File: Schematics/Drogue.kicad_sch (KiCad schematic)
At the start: 7 parts, among them J1 Pyro, Q1 BSC098N10NS5, Q3 NMOS

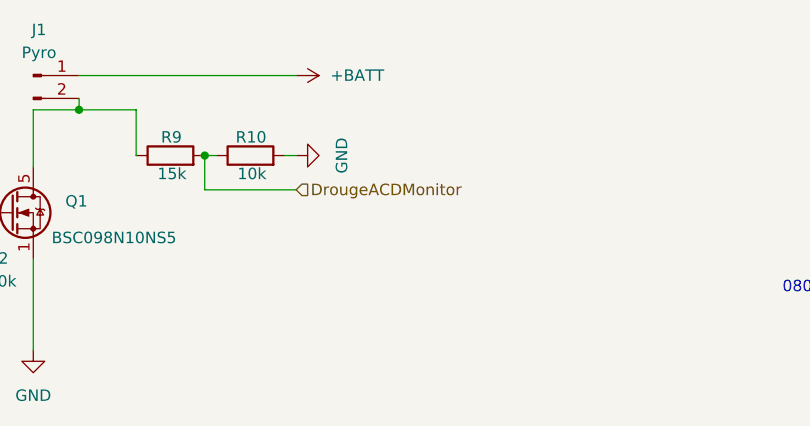
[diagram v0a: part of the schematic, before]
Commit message: finished sensor schematics, added datasheets organized files
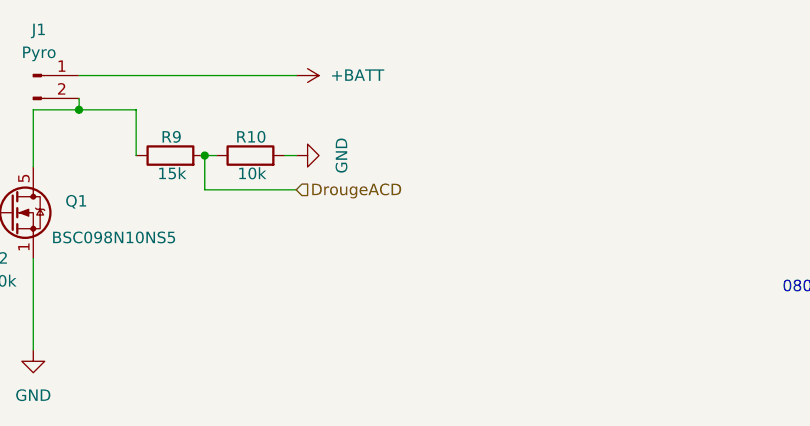
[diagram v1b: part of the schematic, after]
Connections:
- net DrougeACDMonitor renamed DrougeACD
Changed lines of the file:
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@@
 		)
 	)
-	(hierarchical_label "DrougeACDMonitor"
+	(hierarchical_label "DrougeACD"
 		(shape input)
 		(at 160.02 73.66 0)

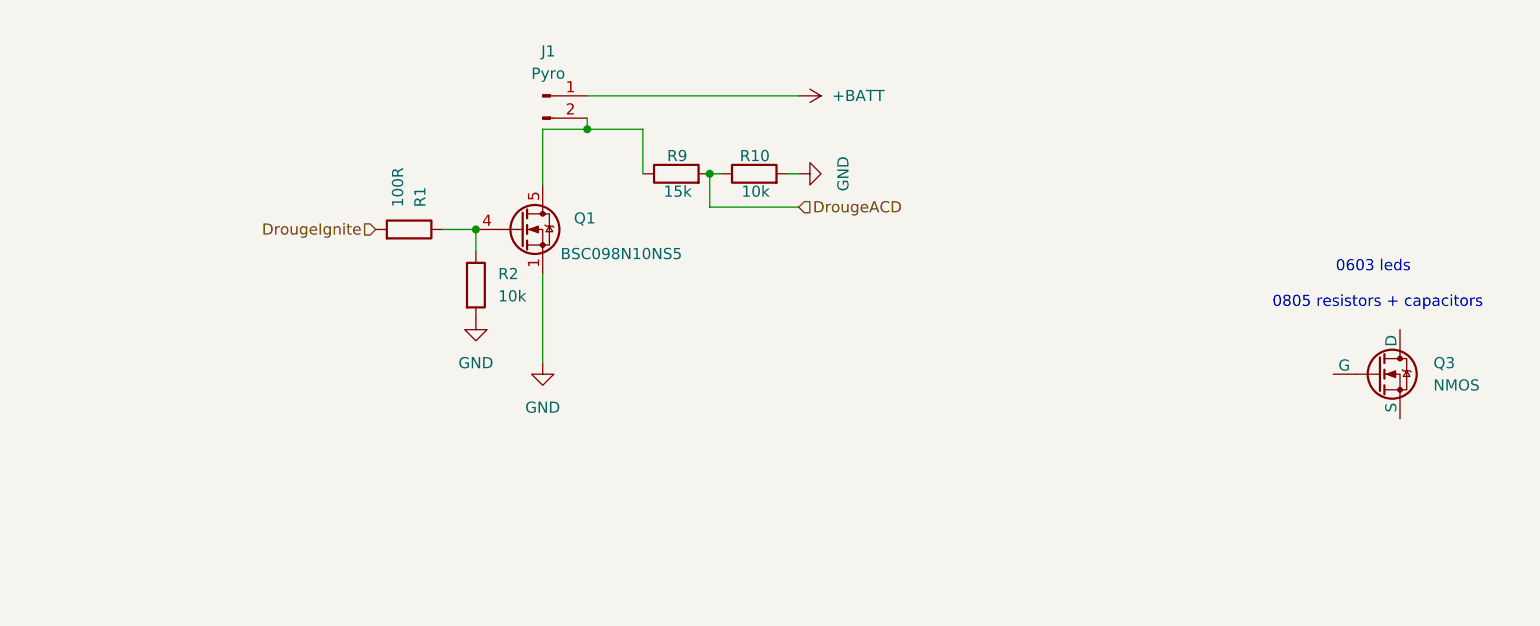
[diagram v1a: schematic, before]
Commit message: added LCSC numbers and footprint values, need to connect schemeatic pins, then can start layout
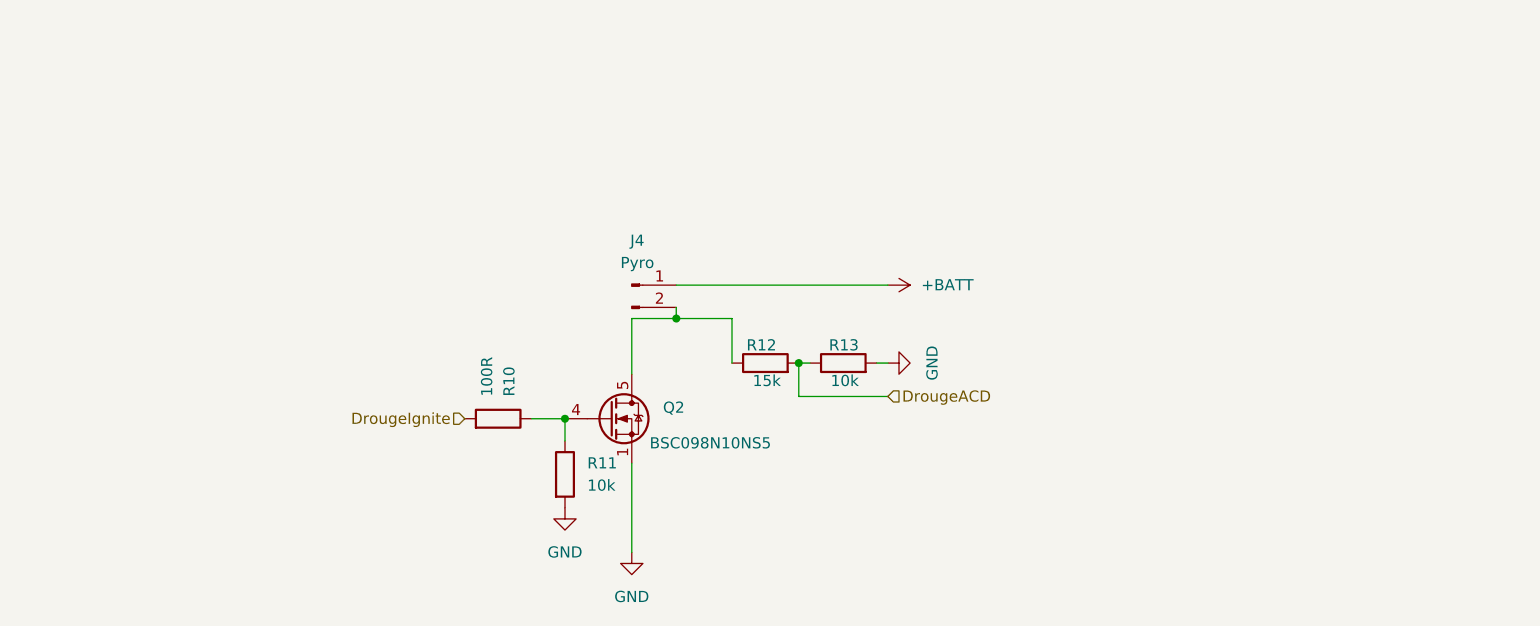
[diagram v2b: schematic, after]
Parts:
- removed Q3: NMOS, symbol Simulation_SPICE:NMOS
- J4: renamed from J1; footprint Connector_Molex:Molex_KK-254_AE-6410-02A_1x02_P2.54mm_Vertical -> myFootprints:MOLEX_26013114; LCSC Part (none) -> C17644051
- Q2: renamed from Q1; LCSC Part (none) -> C534398
- R10: renamed from R1; LCSC Part (none) -> C17408
- R11: renamed from R2; LCSC Part (none) -> C84376
- R12: renamed from R9; footprint Resistor_SMD:R_0805_2012Metric -> Resistor_SMD:R_0805_2012Metric_Pad1.20x1.40mm_HandSolder; LCSC Part (none) -> C2930170
- R13: renamed from R10; LCSC Part (none) -> C84376
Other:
- note removed: "0603 leds"
- note removed: "0805 resistors + capacitors"
- moved on the sheet: J4, Q2, R10, R11, R12, R13

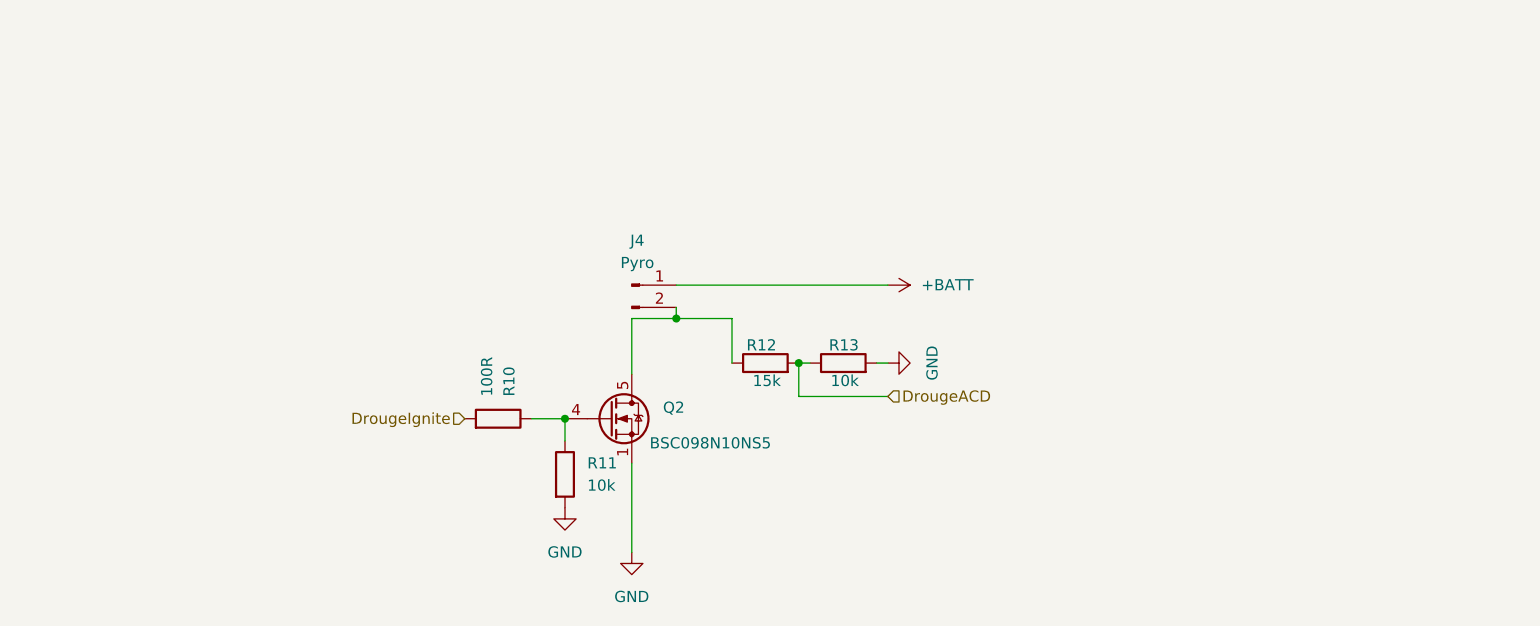
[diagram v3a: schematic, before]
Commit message: fixed symbols and added diodes to power input before ldo
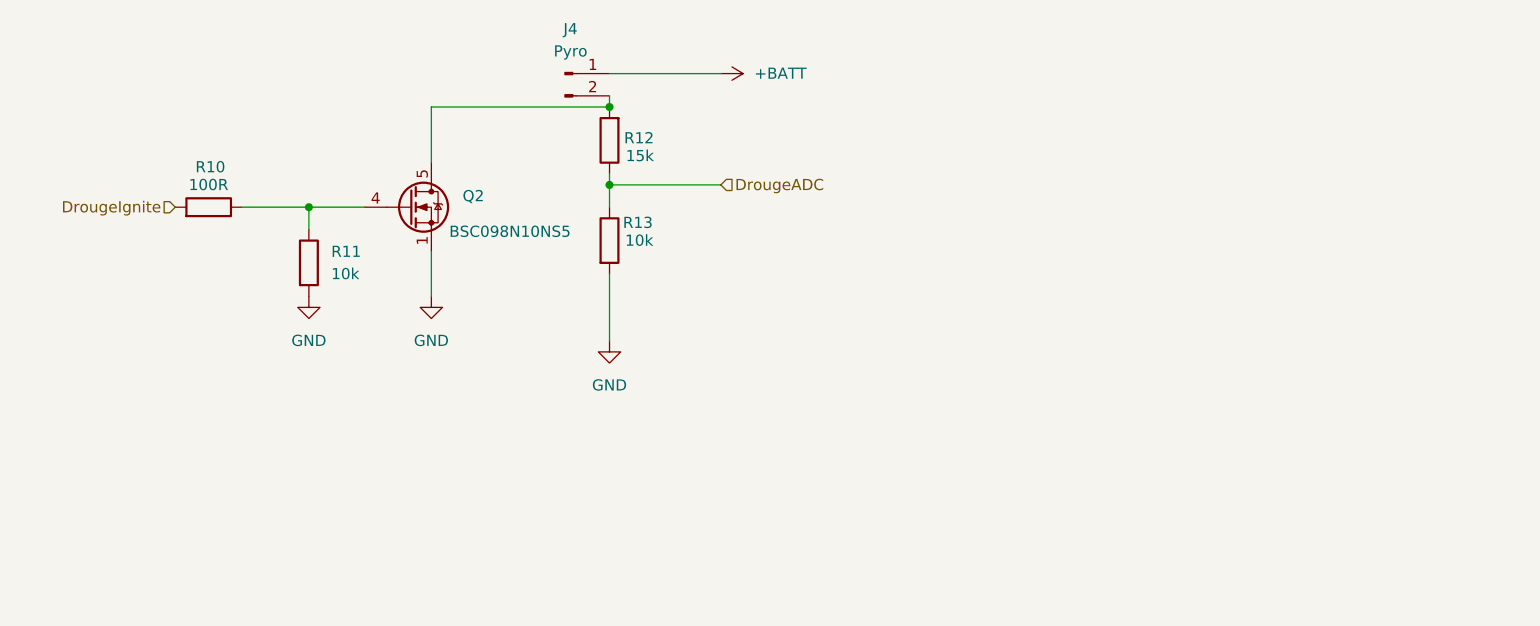
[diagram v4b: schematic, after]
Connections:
- net at J4.2 (Pin_2), Q2.5 (D): now also R12.2; no longer R12.1
- net DrougeACD renamed DrougeADC
- net DrougeADC: now also R12.1; no longer R12.2
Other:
- moved on the sheet: J4, Q2, R10, R11, R12, R13

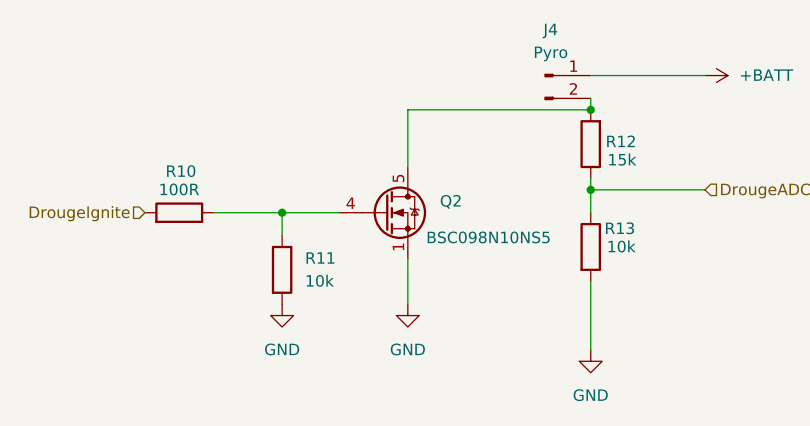
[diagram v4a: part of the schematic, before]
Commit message: added lora correct and organizing sheet pins
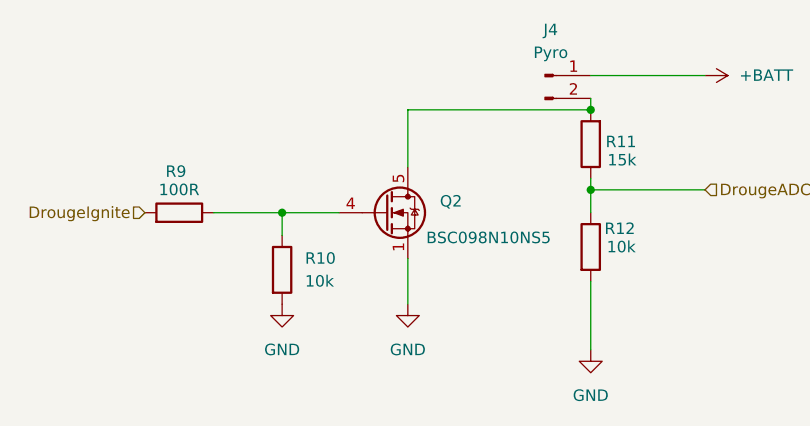
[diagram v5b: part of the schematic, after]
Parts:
- renumbered R11 to R10, R12 to R11, R13 to R12, R10 to R9
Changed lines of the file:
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@@
 		(on_board yes)
 		(dnp no)
-		(property "Reference" "R12"
+		(property "Reference" "R11"
 			(at 143.51 65.786 0)
 			(effects
@@
 			(project "flightcomputer2"
 				(path "/6cb3dda3-5fe8-4715-b831-354360aa3199/49edfe84-9da0-4fce-8baf-f24126c92814"
-					(reference "R12")
+					(reference "R11")
 					(unit 1)
 				)
@@
 		(on_board yes)
 		(dnp no)
-		(property "Reference" "R10"
+		(property "Reference" "R9"
 			(at 91.186 69.088 90)
 			(effects
@@
 			(project "flightcomputer2"
 				(path "/6cb3dda3-5fe8-4715-b831-354360aa3199/49edfe84-9da0-4fce-8baf-f24126c92814"
-					(reference "R10")
+					(reference "R9")
 					(unit 1)
 				)
@@
 		(dnp no)
 		(fields_autoplaced yes)
-		(property "Reference" "R11"
+		(property "Reference" "R10"
 			(at 106.68 78.7399 0)
 			(effects
@@
 			(project "flightcomputer2"
 				(path "/6cb3dda3-5fe8-4715-b831-354360aa3199/49edfe84-9da0-4fce-8baf-f24126c92814"
-					(reference "R11")
+					(reference "R10")
 					(unit 1)
 				)
@@
 		(dnp no)
 		(fields_autoplaced yes)
-		(property "Reference" "#PWR050"
+		(property "Reference" "#PWR047"
 			(at 138.43 95.25 0)
 			(effects
@@
 			(project "flightcomputer2"
 				(path "/6cb3dda3-5fe8-4715-b831-354360aa3199/49edfe84-9da0-4fce-8baf-f24126c92814"
-					(reference "#PWR050")
+					(reference "#PWR047")
 					(unit 1)
 				)
@@
 		(on_board yes)
 		(dnp no)
-		(property "Reference" "R13"
+		(property "Reference" "R12"
 			(at 139.954 75.438 0)
 			(effects
@@
 			(project "flightcomputer2"
 				(path "/6cb3dda3-5fe8-4715-b831-354360aa3199/49edfe84-9da0-4fce-8baf-f24126c92814"
-					(reference "R13")
-					(unit 1)
-				)
+					(reference "R12")
+					(unit 1)
+				)

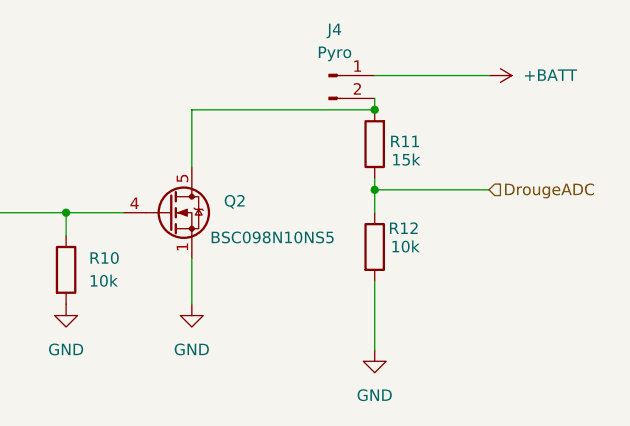
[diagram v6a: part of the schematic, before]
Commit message: first layout need to go over schematic
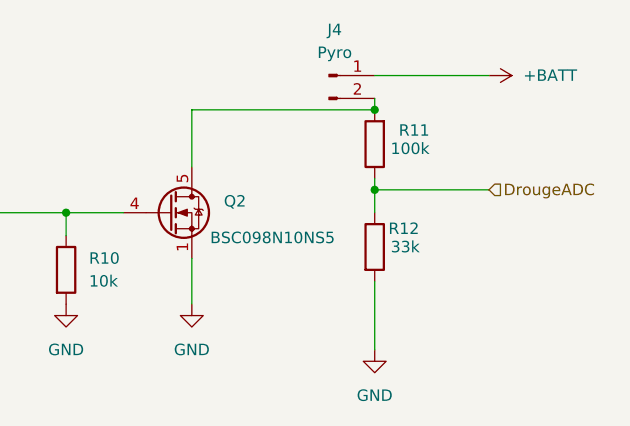
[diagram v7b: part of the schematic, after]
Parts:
- R10, R9: footprint Resistor_SMD:R_0805_2012Metric -> Resistor_SMD:R_0805_2012Metric_Pad1.20x1.40mm_HandSolder
- R11: value 15k -> 100k; LCSC Part C2930170 -> C96346
- R12: value 10k -> 33k; footprint Resistor_SMD:R_0805_2012Metric -> Resistor_SMD:R_0805_2012Metric_Pad1.20x1.40mm_HandSolder; LCSC Part C84376 -> C2933415
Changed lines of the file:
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@@
 		(dnp no)
 		(fields_autoplaced yes)
-		(property "Reference" "#PWR046"
+		(property "Reference" "#PWR052"
 			(at 118.11 90.17 0)
 			(effects
@@
 			(project "flightcomputer2"
 				(path "/6cb3dda3-5fe8-4715-b831-354360aa3199/49edfe84-9da0-4fce-8baf-f24126c92814"
-					(reference "#PWR046")
+					(reference "#PWR052")
 					(unit 1)
 				)
@@
 		(dnp no)
 		(property "Reference" "R11"
-			(at 143.51 65.786 0)
-			(effects
-				(font
-					(size 1.27 1.27)
-				)
-				(justify left)
-			)
-		)
-		(property "Value" "15k"
-			(at 143.51 67.818 0)
+			(at 144.526 64.516 0)
+			(effects
+				(font
+					(size 1.27 1.27)
+				)
+				(justify left)
+			)
+		)
+		(property "Value" "100k"
+			(at 144.526 66.548 0)
 			(effects
 				(font
@@
 			)
 		)
-		(property "LCSC Part" "C2930170"
+		(property "LCSC Part" "C96346"
 			(at 138.43 66.04 90)
 			(effects
@@
 			)
 		)
-		(property "Footprint" "Resistor_SMD:R_0805_2012Metric"
+		(property "Footprint" "Resistor_SMD:R_0805_2012Metric_Pad1.20x1.40mm_HandSolder"
 			(at 92.71 75.438 90)
 			(effects
@@
 			)
 		)
-		(property "Footprint" "Resistor_SMD:R_0805_2012Metric"
+		(property "Footprint" "Resistor_SMD:R_0805_2012Metric_Pad1.20x1.40mm_HandSolder"
 			(at 102.362 80.01 90)
 			(effects
@@
 		(dnp no)
 		(fields_autoplaced yes)
-		(property "Reference" "#PWR047"
+		(property "Reference" "#PWR053"
 			(at 138.43 95.25 0)
 			(effects
@@
 			(project "flightcomputer2"
 				(path "/6cb3dda3-5fe8-4715-b831-354360aa3199/49edfe84-9da0-4fce-8baf-f24126c92814"
-					(reference "#PWR047")
+					(reference "#PWR053")
 					(unit 1)
 				)
@@
 		(dnp no)
 		(fields_autoplaced yes)
-		(property "Reference" "#PWR049"
+		(property "Reference" "#PWR055"
 			(at 147.32 58.42 0)
 			(effects
@@
 			(project ""
 				(path "/6cb3dda3-5fe8-4715-b831-354360aa3199/49edfe84-9da0-4fce-8baf-f24126c92814"
-					(reference "#PWR049")
+					(reference "#PWR055")
 					(unit 1)
 				)
@@
 			)
 		)
-		(property "Value" "10k"
+		(property "Value" "33k"
 			(at 140.208 77.47 0)
 			(effects
@@
 			)
 		)
-		(property "Footprint" "Resistor_SMD:R_0805_2012Metric"
+		(property "Footprint" "Resistor_SMD:R_0805_2012Metric_Pad1.20x1.40mm_HandSolder"
 			(at 136.652 77.47 90)
 			(effects
@@
 			)
 		)
-		(property "LCSC Part" "C84376"
+		(property "LCSC Part" "C2933415"
 			(at 138.43 77.47 90)
 			(effects
@@
 		(dnp no)
 		(fields_autoplaced yes)
-		(property "Reference" "#PWR044"
+		(property "Reference" "#PWR050"
 			(at 104.14 90.17 0)
 			(effects
@@
 			(project "flightcomputer2"
 				(path "/6cb3dda3-5fe8-4715-b831-354360aa3199/49edfe84-9da0-4fce-8baf-f24126c92814"
-					(reference "#PWR044")
+					(reference "#PWR050")
 					(unit 1)
 				)

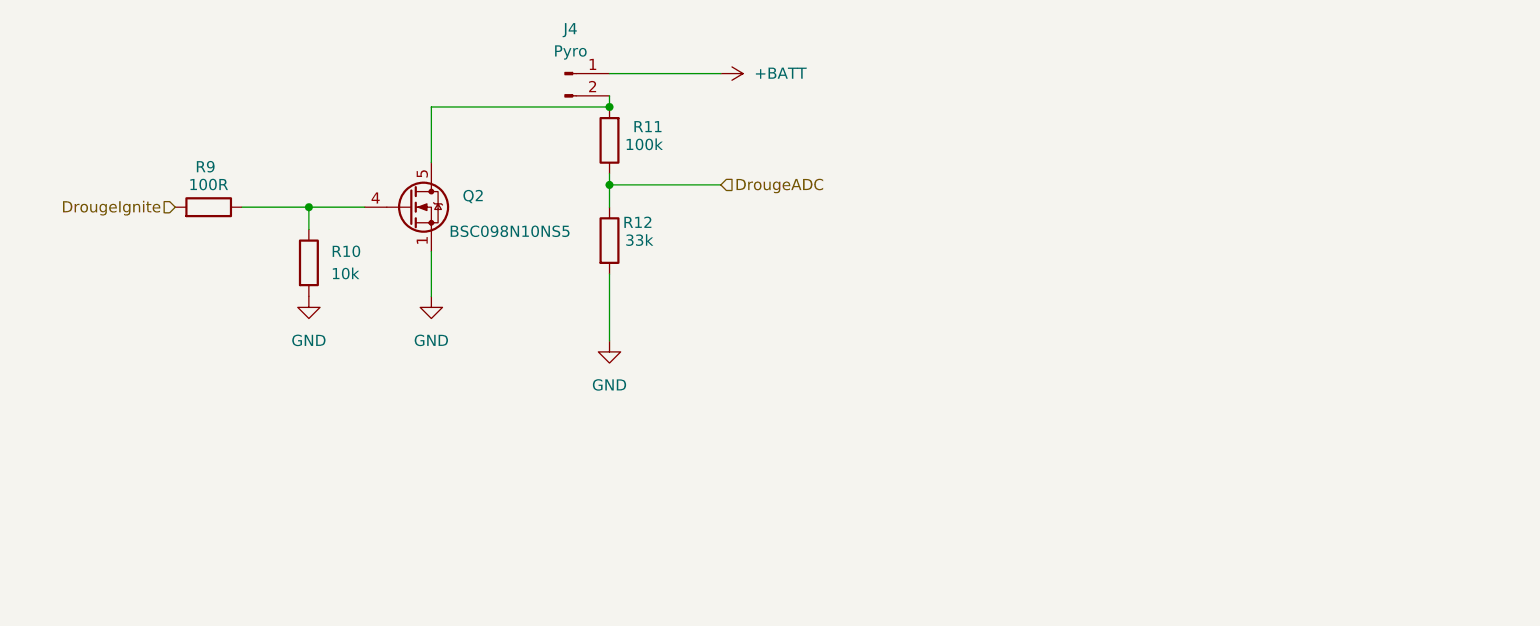
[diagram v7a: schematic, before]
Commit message: began routing, need layout approval
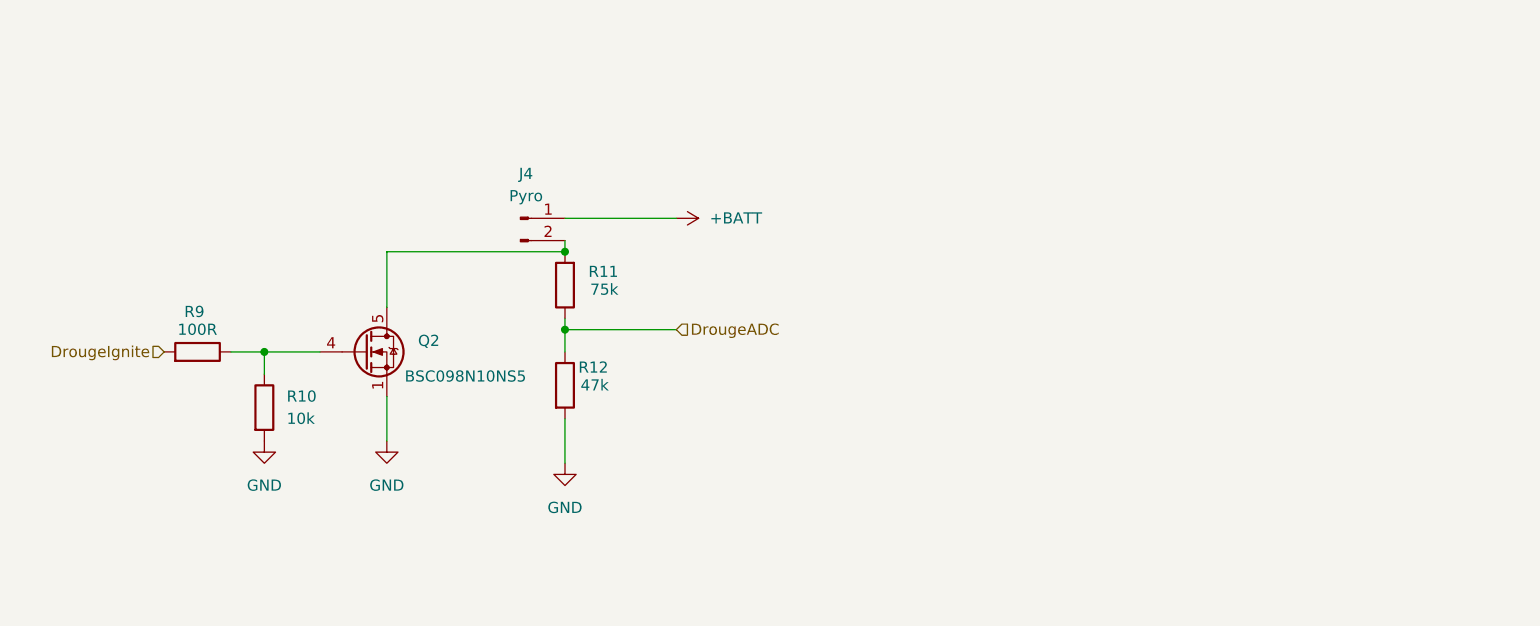
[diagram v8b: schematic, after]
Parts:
- R11: value 100k -> 75k
- R12: value 33k -> 47k
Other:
- moved on the sheet: J4, Q2, R10, R11, R12, R9
